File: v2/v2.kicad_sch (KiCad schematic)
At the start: 105 parts, among them J1 Conn_01x04_Pin, J2 Conn_01x04_Pin, J3 Conn_01x04_Pin, SW1 SW_Push, SW10 SW_Push, SW11 SW_Push, SW12 SW_Push, SW13 SW_Push, SW14 SW_Push, SW15 SW_Push, SW16 SW_Push, SW17 SW_Push, SW18 SW_Push, SW19 SW_Push, SW2 SW_Push, SW20 SW_Push, SW21 SW_Push, SW22 SW_Push, SW23 SW_Push, SW24 SW_Push, SW25 SW_Push, SW26 SW_Push, SW27 SW_Push, SW28 SW_Push, SW29 SW_Push, SW3 SW_Push, SW30 SW_Push, SW31 SW_Push, SW32 SW_Push, SW33 RotaryEncoder_Switch, SW4 SW_Push, SW5 SW_Push, SW6 SW_Push, SW7 SW_Push, SW8 SW_Push, SW9 SW_Push, U1 Pico, U2 Pico

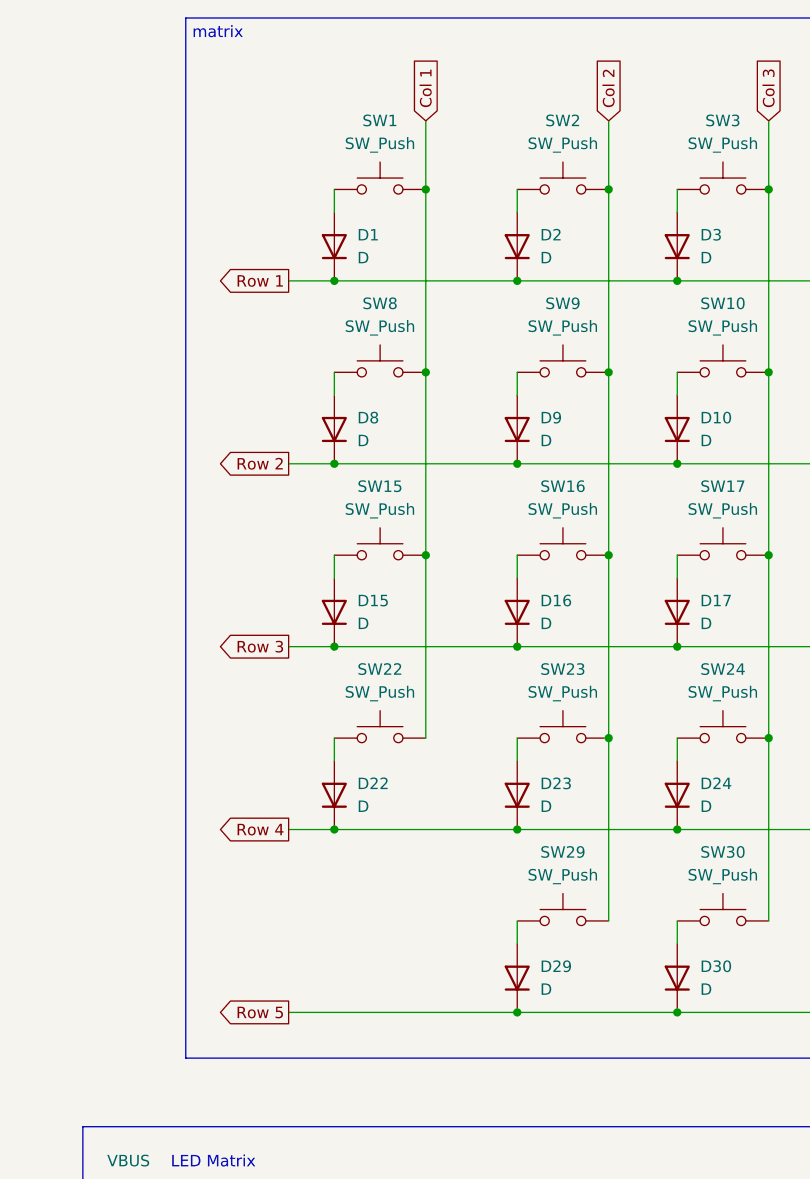
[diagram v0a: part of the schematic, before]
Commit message: finished layout for all components
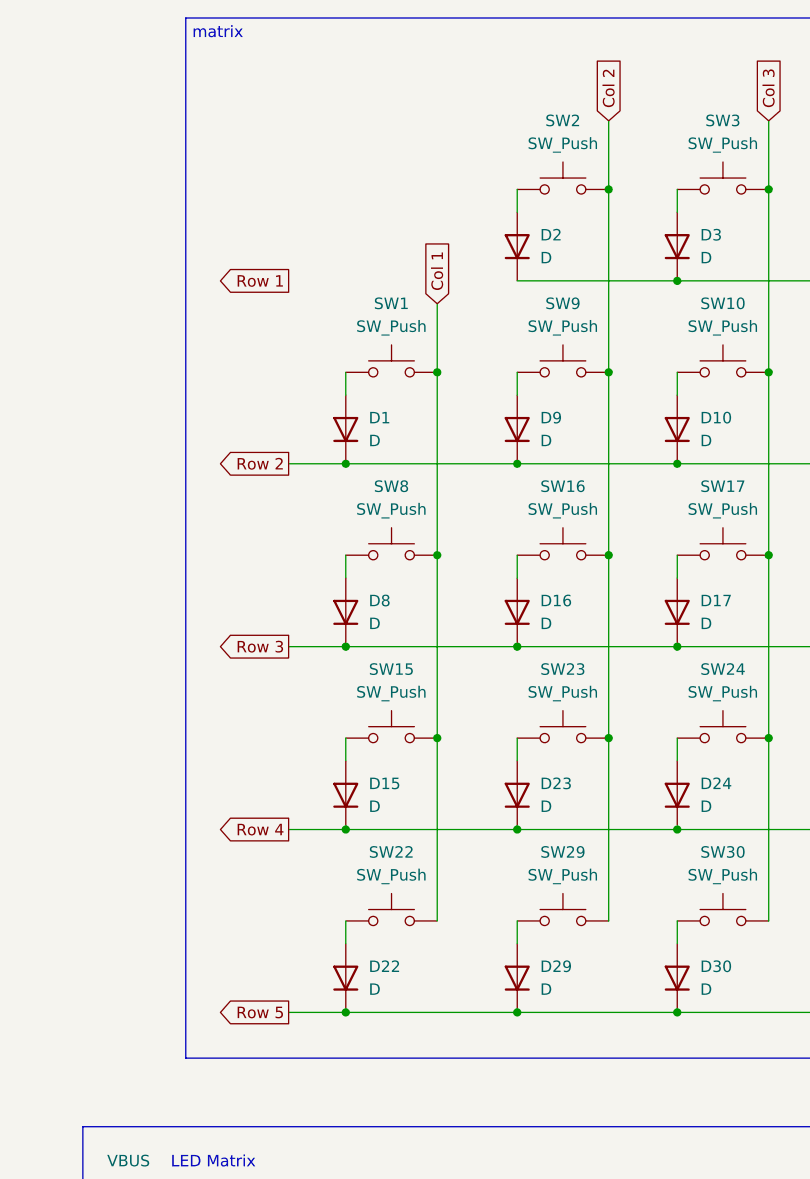
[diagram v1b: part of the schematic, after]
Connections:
- net Row 1: no longer D1.1 (K), D2.1 (K), D3.1 (K), D4.1 (K), D5.1 (K), D6.1 (K), D7.1 (K)
- net Row 2: now also D1.1 (K); no longer D8.1 (K)
- net Row 3: now also D8.1 (K); no longer D15.1 (K)
- net Row 4: now also D15.1 (K); no longer D22.1 (K)
- net Row 5: now also D22.1 (K)
- new net: D2.1 (K), D3.1 (K), D4.1 (K), D5.1 (K), D6.1 (K), D7.1 (K)
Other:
- moved on the sheet: D1, D15, D22, D8, SW1, SW15, SW22, SW8

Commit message: added custom dual side hybrid diode footprint
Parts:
- D1, D10, D11, D12, D13, D14, D15, D16, D17, D18, D19, D2, D20, D21, D22, D23, D24, D25, D26, D27, D28, D29, D3, D30, D31, D32, D33, D4, D5, D6, D7, D8, D9: footprint Keebio-Parts:Diode-Hybrid-Back -> Keebio-Parts:Diode-Hybrid-Dual
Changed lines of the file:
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@@
 			)
 		)
-		(property "Footprint" "Keebio-Parts:Diode-Hybrid-Back"
+		(property "Footprint" "Keebio-Parts:Diode-Hybrid-Dual"
 			(at 265.43 85.09 0)
 			(effects
@@
 			)
 		)
-		(property "Footprint" "Keebio-Parts:Diode-Hybrid-Back"
+		(property "Footprint" "Keebio-Parts:Diode-Hybrid-Dual"
 			(at 227.33 85.09 0)
 			(effects
@@
 			)
 		)
-		(property "Footprint" "Keebio-Parts:Diode-Hybrid-Back"
+		(property "Footprint" "Keebio-Parts:Diode-Hybrid-Dual"
 			(at 152.4 64.77 0)
 			(effects
@@
 			)
 		)
-		(property "Footprint" "Keebio-Parts:Diode-Hybrid-Back"
+		(property "Footprint" "Keebio-Parts:Diode-Hybrid-Dual"
 			(at 208.28 44.45 0)
 			(effects
@@
 			)
 		)
-		(property "Footprint" "Keebio-Parts:Diode-Hybrid-Back"
+		(property "Footprint" "Keebio-Parts:Diode-Hybrid-Dual"
 			(at 246.38 125.73 0)
 			(effects
@@
 			)
 		)
-		(property "Footprint" "Keebio-Parts:Diode-Hybrid-Back"
+		(property "Footprint" "Keebio-Parts:Diode-Hybrid-Dual"
 			(at 227.33 105.41 0)
 			(effects
@@
 			)
 		)
-		(property "Footprint" "Keebio-Parts:Diode-Hybrid-Back"
+		(property "Footprint" "Keebio-Parts:Diode-Hybrid-Dual"
 			(at 152.4 125.73 0)
 			(effects
@@
 			)
 		)
-		(property "Footprint" "Keebio-Parts:Diode-Hybrid-Back"
+		(property "Footprint" "Keebio-Parts:Diode-Hybrid-Dual"
 			(at 246.38 85.09 0)
 			(effects
@@
 			)
 		)
-		(property "Footprint" "Keebio-Parts:Diode-Hybrid-Back"
+		(property "Footprint" "Keebio-Parts:Diode-Hybrid-Dual"
 			(at 171.45 64.77 0)
 			(effects
@@
 			)
 		)
-		(property "Footprint" "Keebio-Parts:Diode-Hybrid-Back"
+		(property "Footprint" "Keebio-Parts:Diode-Hybrid-Dual"
 			(at 189.23 125.73 0)
 			(effects
@@
 			)
 		)
-		(property "Footprint" "Keebio-Parts:Diode-Hybrid-Back"
+		(property "Footprint" "Keebio-Parts:Diode-Hybrid-Dual"
 			(at 265.43 44.45 0)
 			(effects
@@
 			)
 		)
-		(property "Footprint" "Keebio-Parts:Diode-Hybrid-Back"
+		(property "Footprint" "Keebio-Parts:Diode-Hybrid-Dual"
 			(at 208.28 64.77 0)
 			(effects
@@
 			)
 		)
-		(property "Footprint" "Keebio-Parts:Diode-Hybrid-Back"
+		(property "Footprint" "Keebio-Parts:Diode-Hybrid-Dual"
 			(at 189.23 85.09 0)
 			(effects
@@
 			)
 		)
-		(property "Footprint" "Keebio-Parts:Diode-Hybrid-Back"
+		(property "Footprint" "Keebio-Parts:Diode-Hybrid-Dual"
 			(at 265.43 105.41 0)
 			(effects
@@
 			)
 		)
-		(property "Footprint" "Keebio-Parts:Diode-Hybrid-Back"
+		(property "Footprint" "Keebio-Parts:Diode-Hybrid-Dual"
 			(at 189.23 64.77 0)
 			(effects
@@
 			)
 		)
-		(property "Footprint" "Keebio-Parts:Diode-Hybrid-Back"
+		(property "Footprint" "Keebio-Parts:Diode-Hybrid-Dual"
 			(at 208.28 85.09 0)
 			(effects
@@
 			)
 		)
-		(property "Footprint" "Keebio-Parts:Diode-Hybrid-Back"
+		(property "Footprint" "Keebio-Parts:Diode-Hybrid-Dual"
 			(at 246.38 64.77 0)
 			(effects
@@
 			)
 		)
-		(property "Footprint" "Keebio-Parts:Diode-Hybrid-Back"
+		(property "Footprint" "Keebio-Parts:Diode-Hybrid-Dual"
 			(at 208.28 125.73 0)
 			(effects
@@
 			)
 		)
-		(property "Footprint" "Keebio-Parts:Diode-Hybrid-Back"
+		(property "Footprint" "Keebio-Parts:Diode-Hybrid-Dual"
 			(at 208.28 105.41 0)
 			(effects
@@
 			)
 		)
-		(property "Footprint" "Keebio-Parts:Diode-Hybrid-Back"
+		(property "Footprint" "Keebio-Parts:Diode-Hybrid-Dual"
 			(at 171.45 44.45 0)
 			(effects
@@
 			)
 		)
-		(property "Footprint" "Keebio-Parts:Diode-Hybrid-Back"
+		(property "Footprint" "Keebio-Parts:Diode-Hybrid-Dual"
 			(at 227.33 44.45 0)
 			(effects
@@
 			)
 		)
-		(property "Footprint" "Keebio-Parts:Diode-Hybrid-Back"
+		(property "Footprint" "Keebio-Parts:Diode-Hybrid-Dual"
 			(at 246.38 105.41 0)
 			(effects
@@
 			)
 		)
-		(property "Footprint" "Keebio-Parts:Diode-Hybrid-Back"
+		(property "Footprint" "Keebio-Parts:Diode-Hybrid-Dual"
 			(at 227.33 64.77 0)
 			(effects
@@
 			)
 		)
-		(property "Footprint" "Keebio-Parts:Diode-Hybrid-Back"
+		(property "Footprint" "Keebio-Parts:Diode-Hybrid-Dual"
 			(at 227.33 125.73 0)
 			(effects
@@
 			)
 		)
-		(property "Footprint" "Keebio-Parts:Diode-Hybrid-Back"
+		(property "Footprint" "Keebio-Parts:Diode-Hybrid-Dual"
 			(at 171.45 125.73 0)
 			(effects
@@
 			)
 		)
-		(property "Footprint" "Keebio-Parts:Diode-Hybrid-Back"
+		(property "Footprint" "Keebio-Parts:Diode-Hybrid-Dual"
 			(at 152.4 105.41 0)
 			(effects
@@
 			)
 		)
-		(property "Footprint" "Keebio-Parts:Diode-Hybrid-Back"
+		(property "Footprint" "Keebio-Parts:Diode-Hybrid-Dual"
 			(at 152.4 85.09 0)
 			(effects
@@
 			)
 		)
-		(property "Footprint" "Keebio-Parts:Diode-Hybrid-Back"
+		(property "Footprint" "Keebio-Parts:Diode-Hybrid-Dual"
 			(at 171.45 85.09 0)
 			(effects
@@
 			)
 		)
-		(property "Footprint" "Keebio-Parts:Diode-Hybrid-Back"
+		(property "Footprint" "Keebio-Parts:Diode-Hybrid-Dual"
 			(at 189.23 44.45 0)
 			(effects
@@
 			)
 		)
-		(property "Footprint" "Keebio-Parts:Diode-Hybrid-Back"
+		(property "Footprint" "Keebio-Parts:Diode-Hybrid-Dual"
 			(at 265.43 64.77 0)
 			(effects
@@
 			)
 		)
-		(property "Footprint" "Keebio-Parts:Diode-Hybrid-Back"
+		(property "Footprint" "Keebio-Parts:Diode-Hybrid-Dual"
 			(at 189.23 105.41 0)
 			(effects
@@
 			)
 		)
-		(property "Footprint" "Keebio-Parts:Diode-Hybrid-Back"
+		(property "Footprint" "Keebio-Parts:Diode-Hybrid-Dual"
 			(at 246.38 44.45 0)
 			(effects
@@
 			)
 		)
-		(property "Footprint" "Keebio-Parts:Diode-Hybrid-Back"
+		(property "Footprint" "Keebio-Parts:Diode-Hybrid-Dual"
 			(at 171.45 105.41 0)
 			(effects

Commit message: started running traces
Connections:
- net +3.3V: now also U1.36 (3V3)
- net ENC A: now also U1.32 (GPIO27_ADC1), U2.32 (GPIO27_ADC1)
- net ENC B: now also U1.31 (GPIO26_ADC0), U2.31 (GPIO26_ADC0)
- net Row 1: now also D2.1 (K), D3.1 (K), D4.1 (K), D5.1 (K), D6.1 (K), D7.1 (K)
- net SERIAL A: now also U2.25 (GPIO19)
- net SERIAL B: now also U2.24 (GPIO18)

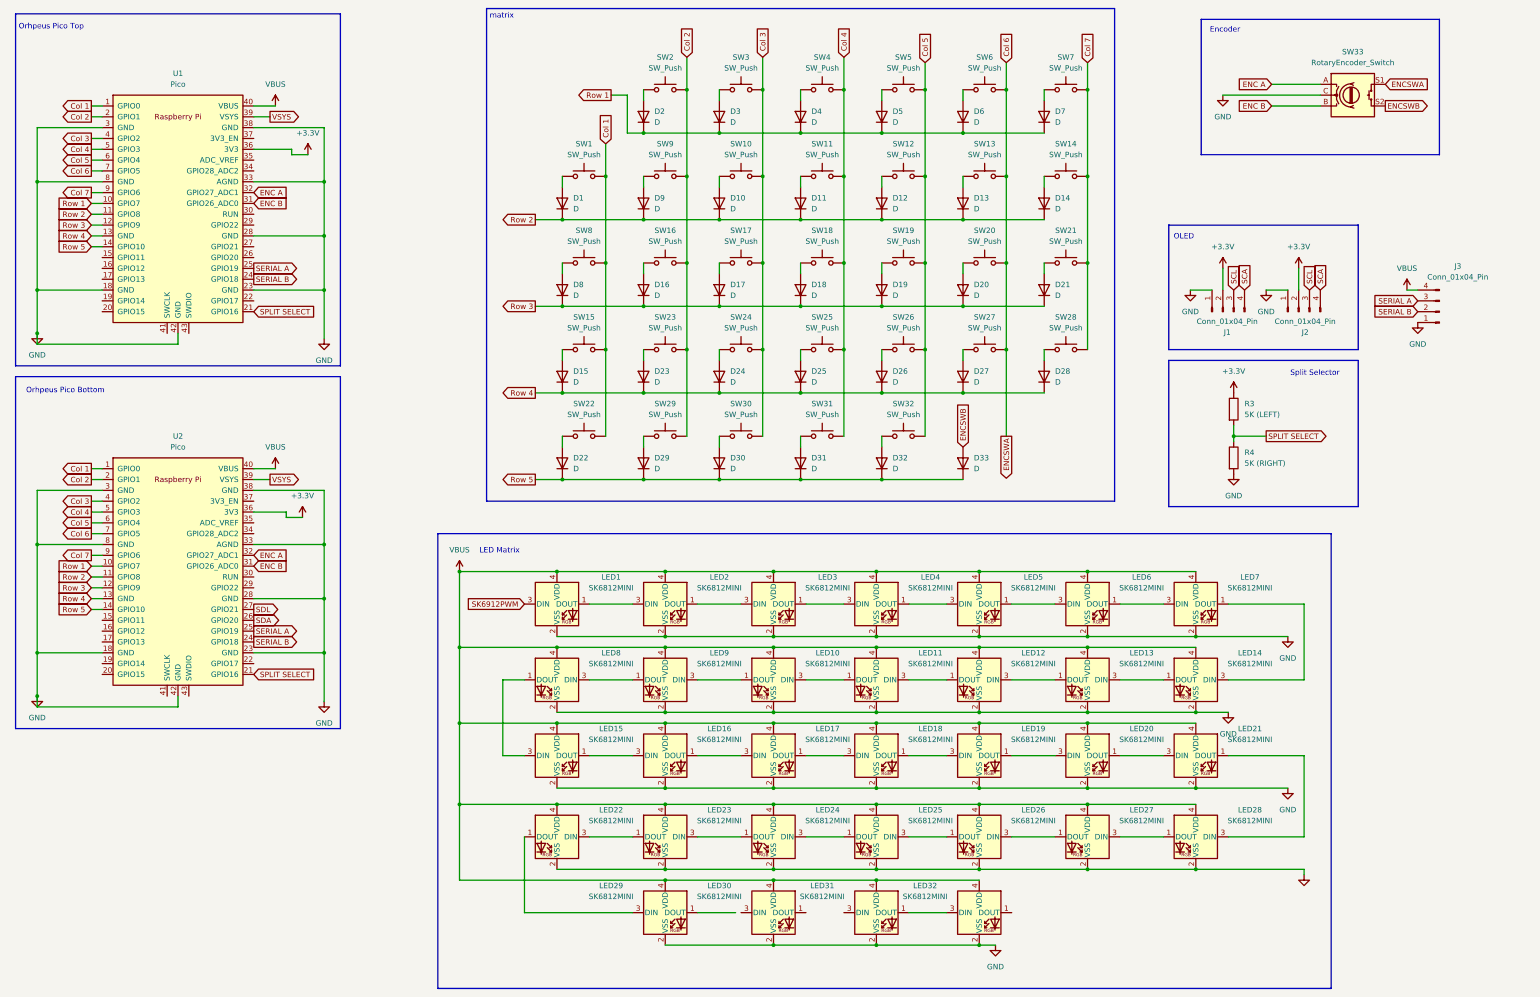
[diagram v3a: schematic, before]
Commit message: redo some schematics, time to redo LEDs
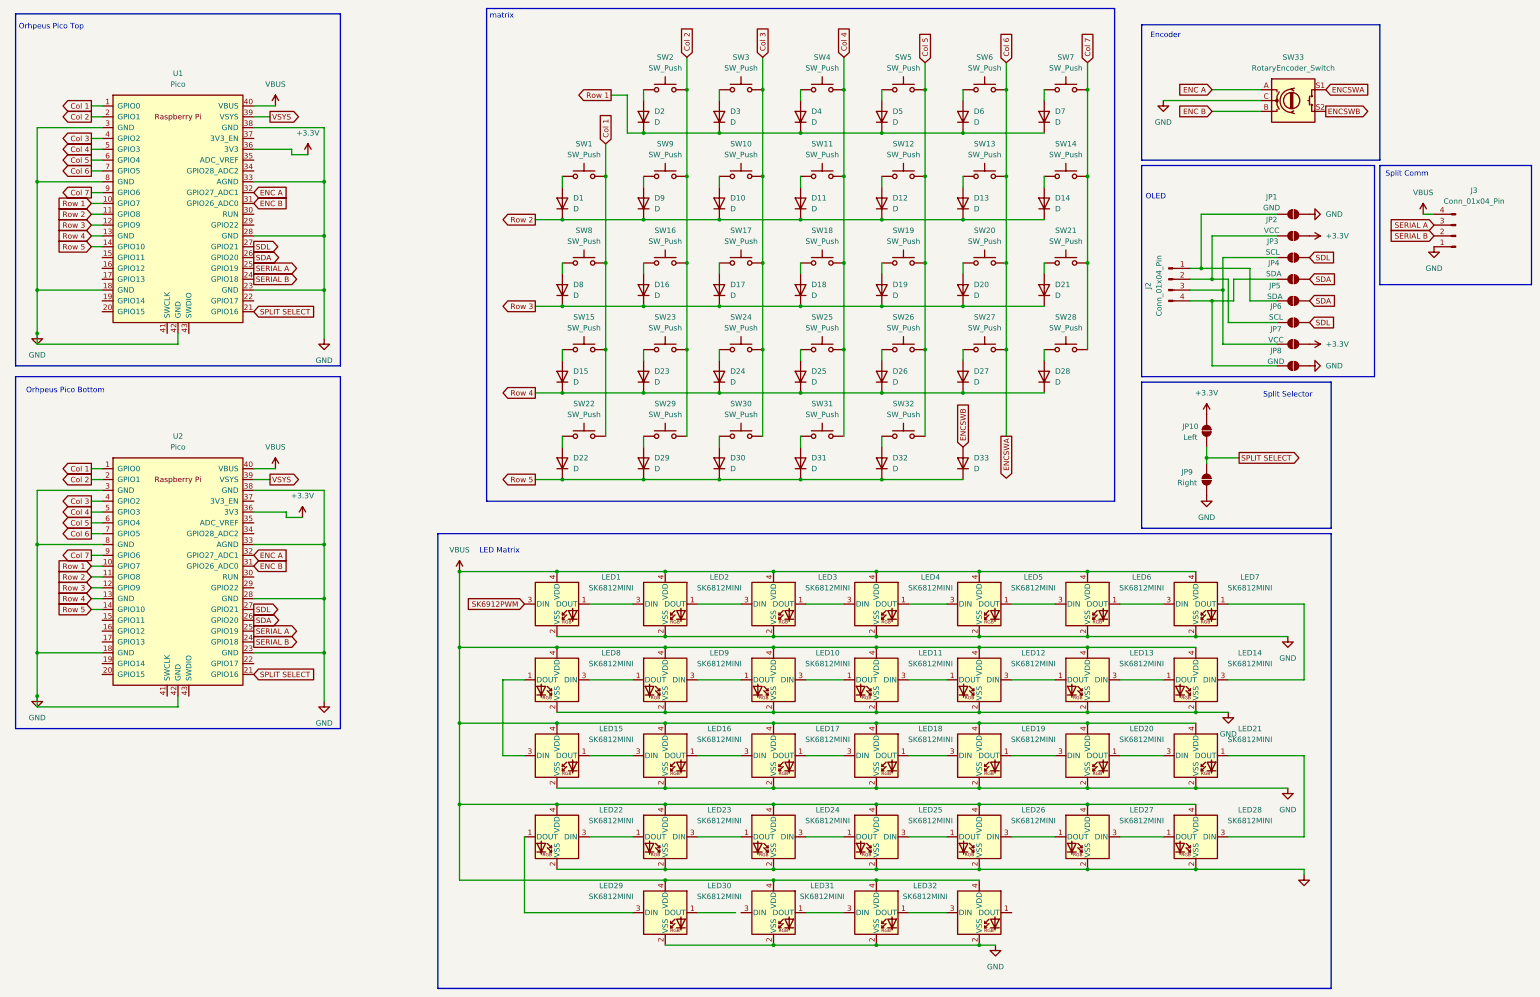
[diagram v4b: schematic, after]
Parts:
- removed J1: Conn_01x04_Pin, Keebio-Parts:I2C_Breakout, symbol Connector:Conn_01x04_Pin
- removed R3: 5K (LEFT), Keebio-Parts:Resistor, symbol Device:R
- removed R4: 5K (RIGHT), Keebio-Parts:Resistor, symbol Device:R
- added JP1, JP8: GND, Keebio-Parts:solder_jumper, symbol Jumper:SolderJumper_2_Open
- added JP10: Left, Keebio-Parts:solder_jumper, symbol Jumper:SolderJumper_2_Open
- added JP2, JP7: VCC, Keebio-Parts:solder_jumper, symbol Jumper:SolderJumper_2_Open
- added JP3, JP6: SCL, Keebio-Parts:solder_jumper, symbol Jumper:SolderJumper_2_Open
- added JP4, JP5: SDA, Keebio-Parts:solder_jumper, symbol Jumper:SolderJumper_2_Open
- added JP9: Right, Keebio-Parts:solder_jumper, symbol Jumper:SolderJumper_2_Open
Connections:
- net +3.3V: now also JP10.2 (B), JP2.2 (B), JP7.2 (B); no longer J2.2 (Pin_2)
- net GND: now also JP1.2 (B), JP8.2 (B), JP9.1 (A); no longer J2.1 (Pin_1)
- net SDA: now also U1.26 (GPIO20), JP4.2 (B), JP5.2 (B)
- net SDL: now also U1.27 (GPIO21), JP3.2 (B), JP6.2 (B)
- net SPLIT SELECT: now also JP10.1 (A), JP9.2 (B)
- net at LED31.3 (DIN): now also LED30.1 (DOUT)
- net SCA: no longer names the net of J2.4 (Pin_4)
- net SCA: now also JP4.1 (A), JP8.1 (A)
- net SCL: no longer names the net of J2.3 (Pin_3)
- net SCL: now also JP3.1 (A), JP7.1 (A)
- new net: J2.2 (Pin_2), JP2.1 (A), JP6.1 (A)
- new net: J2.1 (Pin_1), JP1.1 (A), JP5.1 (A)
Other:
- note added: "Split Comm"
- moved on the sheet: J2, J3, SW33

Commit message: finished routing and make fill zones
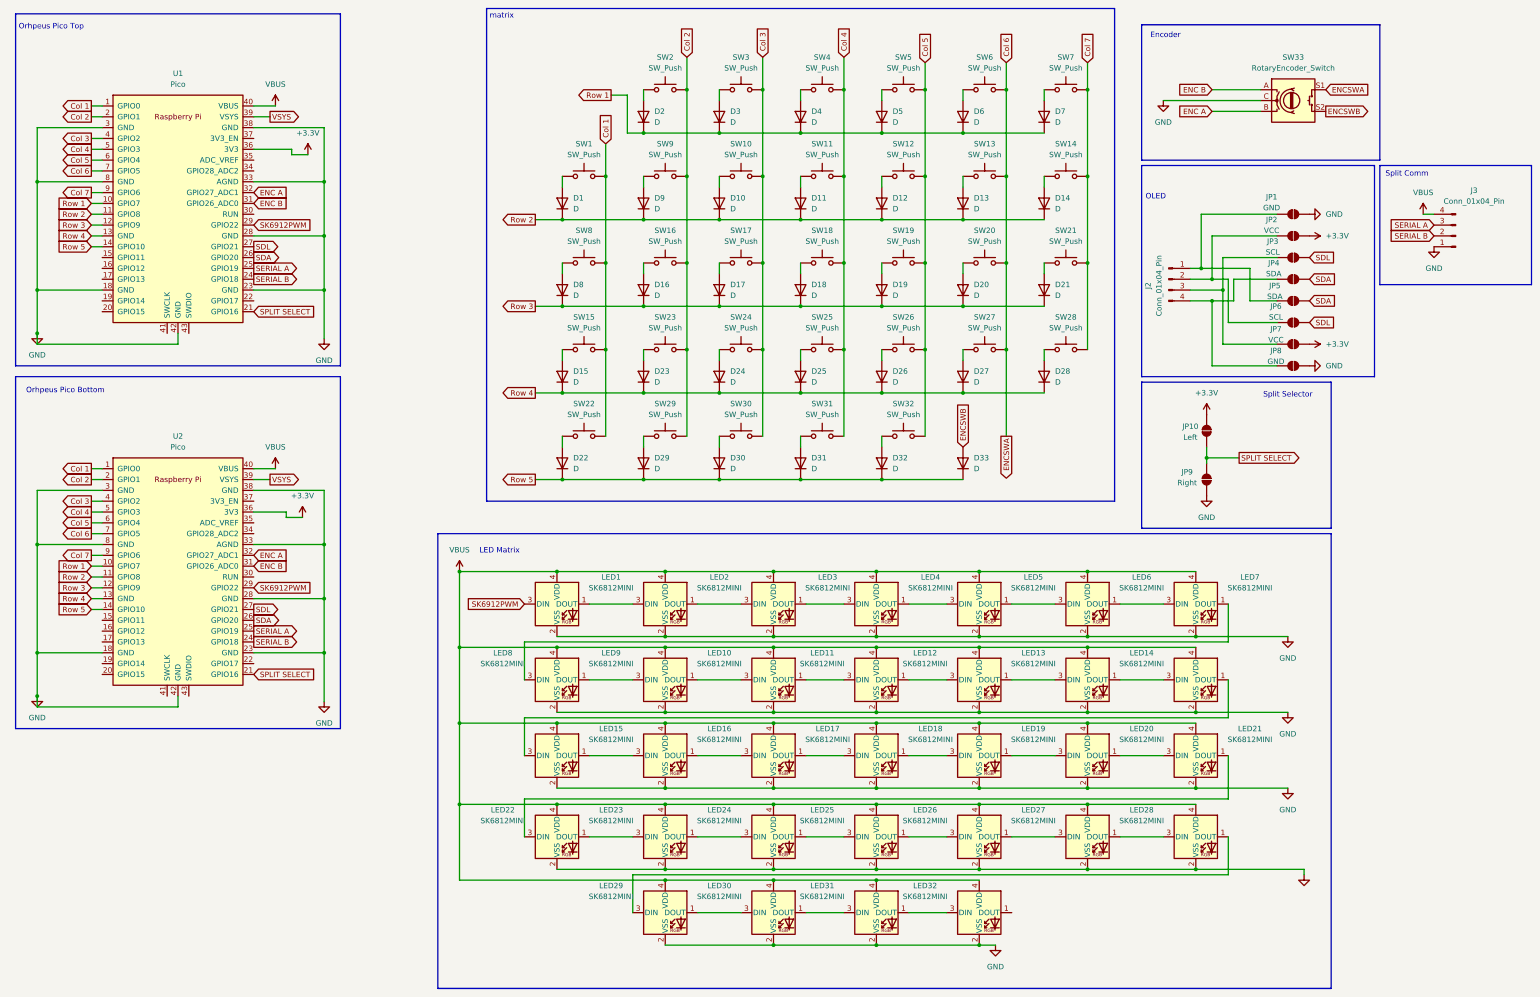
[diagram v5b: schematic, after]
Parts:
- JP1, JP10, JP2, JP3, JP4, JP5, JP6, JP7, JP8, JP9: footprint Keebio-Parts:solder_jumper -> Jumper:SolderJumper-2_P1.3mm_Open_RoundedPad1.0x1.5mm
- renumbered LED12 to LED10, LED10 to LED12, LED9 to LED13, LED8 to LED14, LED28 to LED22, LED27 to LED23, LED26 to LED24, LED24 to LED26, LED23 to LED27, LED22 to LED28, LED14 to LED8, LED13 to LED9
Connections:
- net ENC A: now also SW33.B; no longer SW33.A
- net ENC B: now also SW33.A; no longer SW33.B
- net SK6912PWM: now also U1.29 (GPIO22), U2.29 (GPIO22)
- net at LED29.1 (DOUT): now also LED30.3 (DIN)
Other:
- moved on the sheet: LED10, LED12, LED13, LED14, LED22, LED23, LED24, LED26, LED27, LED28, LED8, LED9
